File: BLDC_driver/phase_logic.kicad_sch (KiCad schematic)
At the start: 66 parts, among them Q1 AOTL66912, Q2 AOTL66912, Q3 AOTL66912, Q4 AOTL66912, Q5 AOTL66912, Q6 AOTL66912

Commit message: Layout progress
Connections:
- net A_CSN is gone; now on net A_CSP: R13.1
- net B_CSN is gone; now on net B_CSP: R14.1
- net C_CSN is gone; now on net C_CSP: R15.1
- net A_CSP: now also C13.2, Q6.2 (S); no longer R13.2 (4)
- net B_CSP: now also C14.2, Q5.2 (S); no longer R14.2 (4)
- net C_CSP: now also C15.2, Q4.2 (S); no longer R15.2 (4)
- net GND: now also R13.2, R14.2, R15.2; no longer R13.1 (2), R14.1 (2), R15.1 (2)

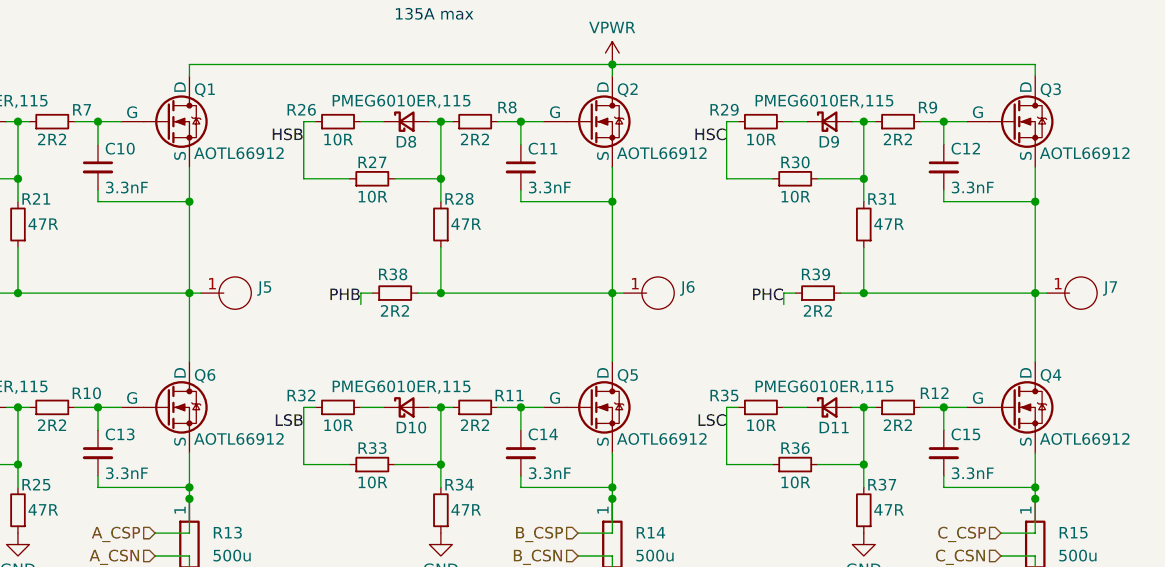
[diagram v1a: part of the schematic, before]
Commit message: Rough inverter stage layout
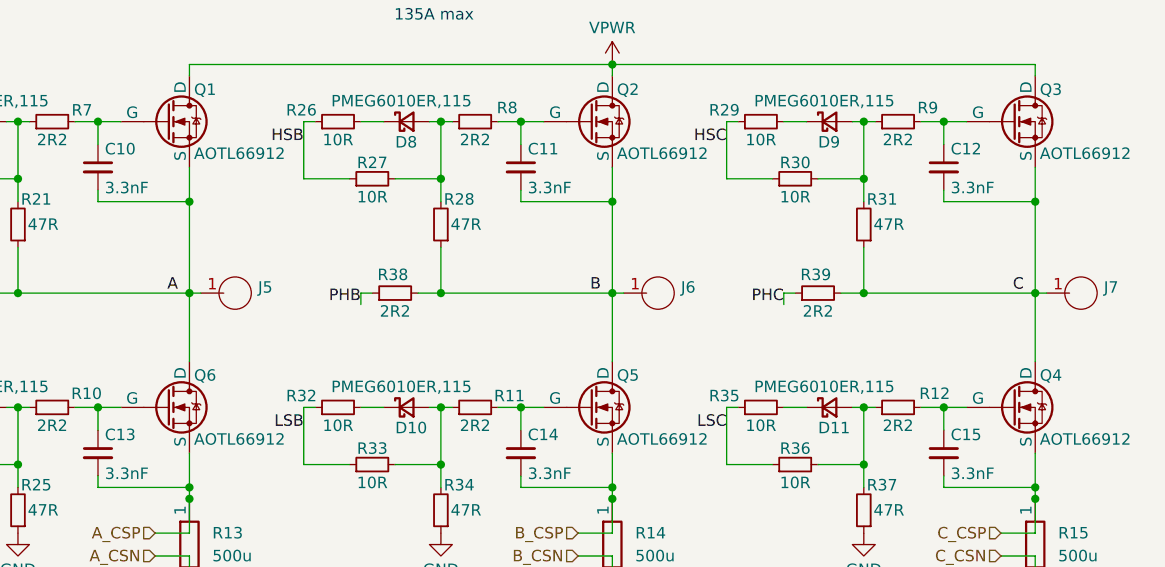
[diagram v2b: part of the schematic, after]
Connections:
- net A: now reaches C10.2, J5.1, Q1.2 (S), Q6.3 (D), R21.1, R22.2
- net B: now reaches C11.2, J6.1, Q2.2 (S), Q5.3 (D), R28.1, R38.2
- net C: now reaches C12.2, J7.1, Q3.2 (S), Q4.3 (D), R31.1, R39.2
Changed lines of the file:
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@@
+		)
+	)
+	(label "C"
+		(at 204.47 63.5 180)
+		(fields_autoplaced yes)
+		(effects
+			(font
+				(size 1.27 1.27)
+			)
+			(justify right bottom)
 		)
 	)
@@
 		)
 	)
+	(label "A"
+		(at 110.49 63.5 180)
+		(fields_autoplaced yes)
+		(effects
+			(font
+				(size 1.27 1.27)
+			)
+			(justify right bottom)
+		)
+	)
 	(label "LSA"
 		(at 49.53 127 180)
@@
 		)
 	)
+	(label "B"
+		(at 157.48 63.5 180)
+		(fields_autoplaced yes)
+		(effects
+			(font
+				(size 1.27 1.27)
+			)
+			(justify right bottom)
+		)
+	)

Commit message: Layout progress
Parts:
- R13, R14, R15: value 500u -> 200u
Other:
- note added: "360A max?"
- note removed: "135A max"
- note removed: "Connectors valid and rated for 110A??"
- note removed: "TODO: SHUNT RESISTORS!!!"
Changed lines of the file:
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@@
 		)
 	)
-	(text "TODO: SHUNT RESISTORS!!!"
-		(exclude_from_sim no)
-		(at 179.578 100.838 0)
-		(effects
-			(font
-				(size 1.27 1.27)
-			)
-		)
-	)
-	(text "135A max"
+	(text "360A max?"
 		(exclude_from_sim no)
 		(at 138.938 32.766 0)
@@
 		)
 	)
-	(text "Connectors valid and rated for 110A??"
-		(exclude_from_sim no)
-		(at 150.368 108.204 0)
-		(effects
-			(font
-				(size 1.27 1.27)
-			)
-		)
-	)
 	(label "C"
 		(at 204.47 63.5 180)
@@
 			)
 		)
-		(property "Value" "500u"
+		(property "Value" "200u"
 			(at 161.29 92.7099 0)
 			(effects
@@
 			)
 		)
-		(property "Value" "500u"
+		(property "Value" "200u"
 			(at 208.28 92.7099 0)
 			(effects
@@
 			)
 		)
-		(property "Value" "500u"
+		(property "Value" "200u"
 			(at 114.3 92.7099 0)
 			(effects
